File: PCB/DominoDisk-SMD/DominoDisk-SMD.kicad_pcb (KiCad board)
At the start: 4 copper layers, 44 x 32.6 mm, 31 parts, among them J1 Daisy port out, J2 ICSP_ISP6, J3 Daisy port in, J4 UART, K1 TF-104 MicroSD card holder, U1 PC817C-S, U2 ATmega328P-AU, U3 TXB0104PWR level shifter, U4 SE5218ALG voltage regulator, Y1 CSTNE16M0V530000R0 Resonator

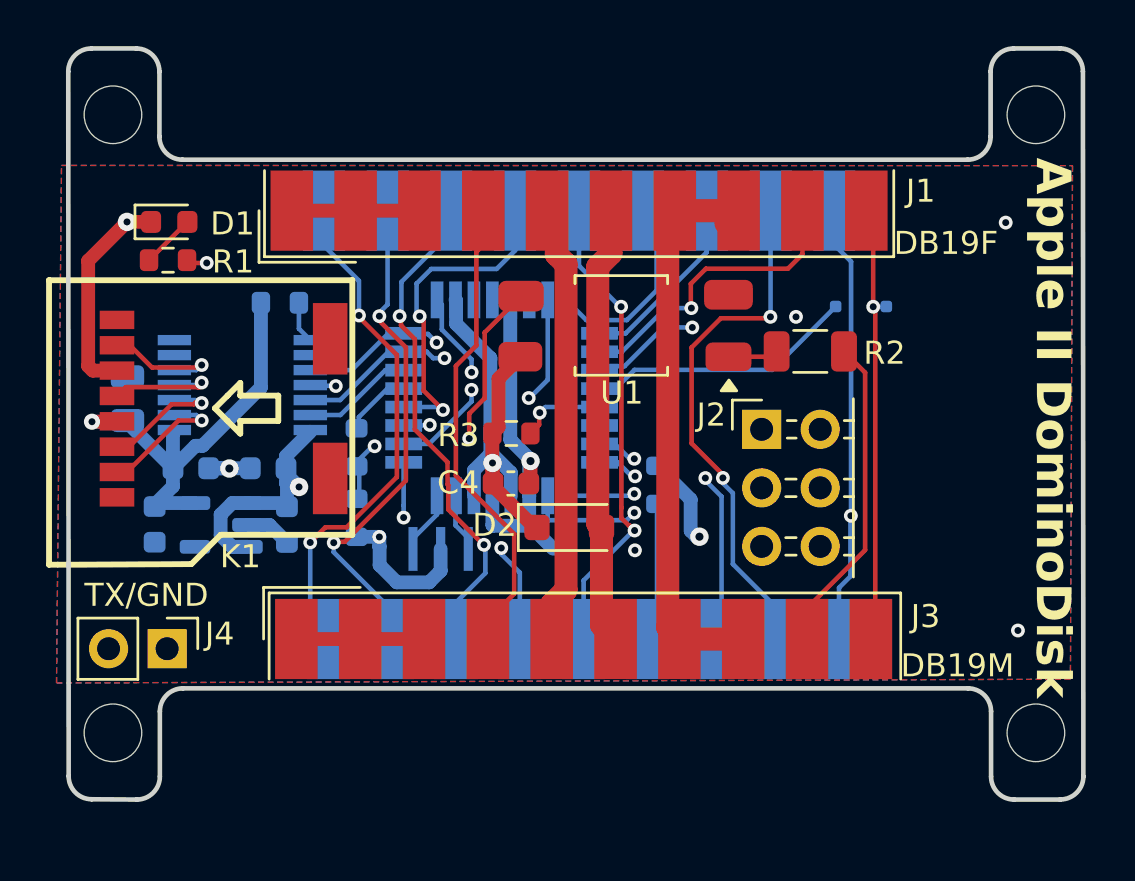
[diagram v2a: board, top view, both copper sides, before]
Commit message: Silkscreen/via avoidance
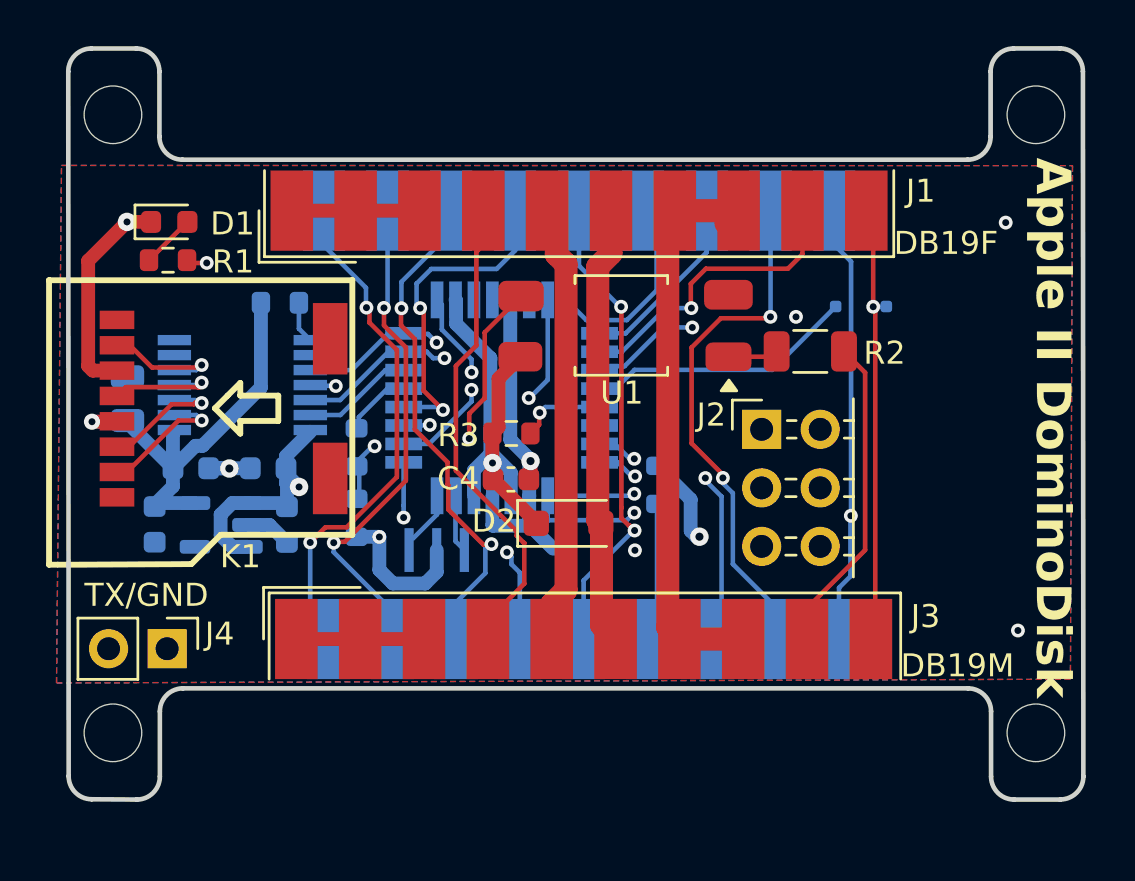
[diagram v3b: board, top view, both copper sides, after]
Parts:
- moved D2 0.18 mm to (121.6, 59.9)
- moved C4 0.18 mm to (119.1, 58.0)
- moved Y1 0.18 mm to (115.9, 61.1)

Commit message: Add via/silkscreen DRC
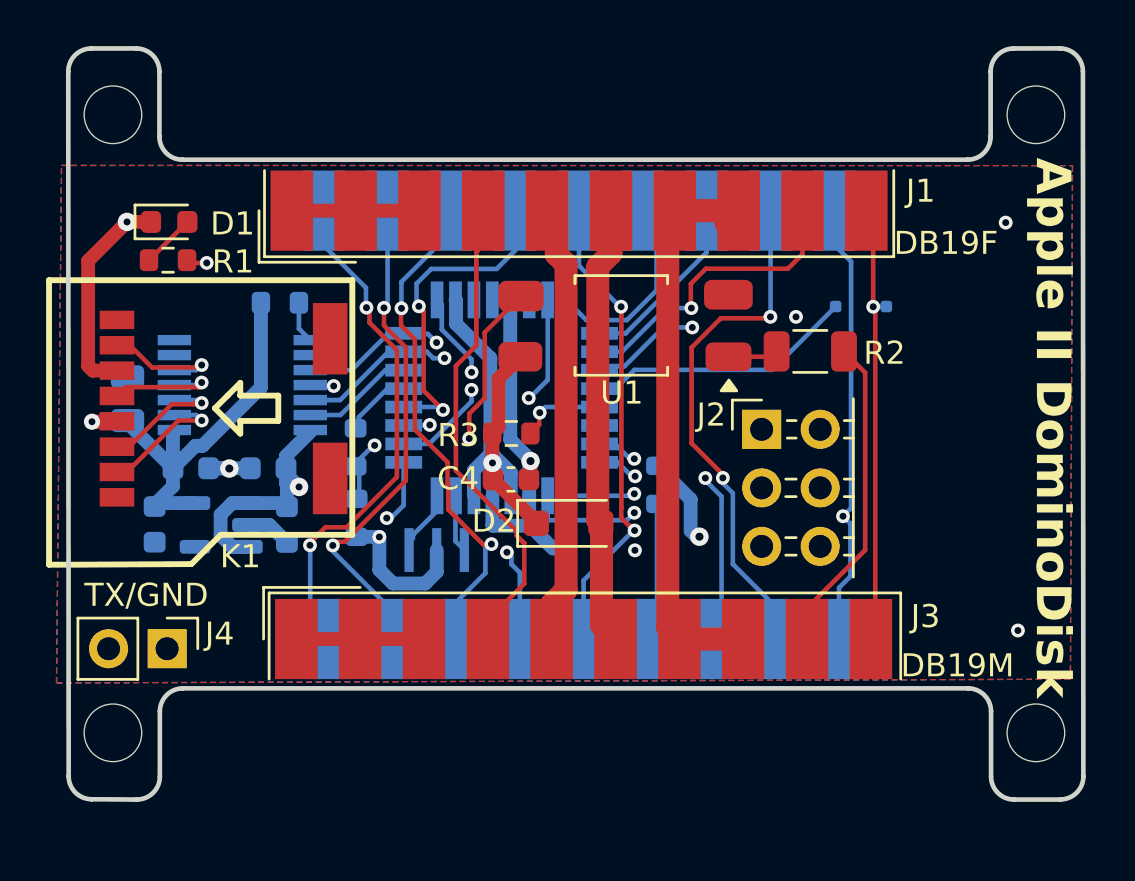
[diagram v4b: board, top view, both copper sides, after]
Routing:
- net PH3_in: track 11.7 -> 12.9 mm

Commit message: Make a full ground plane
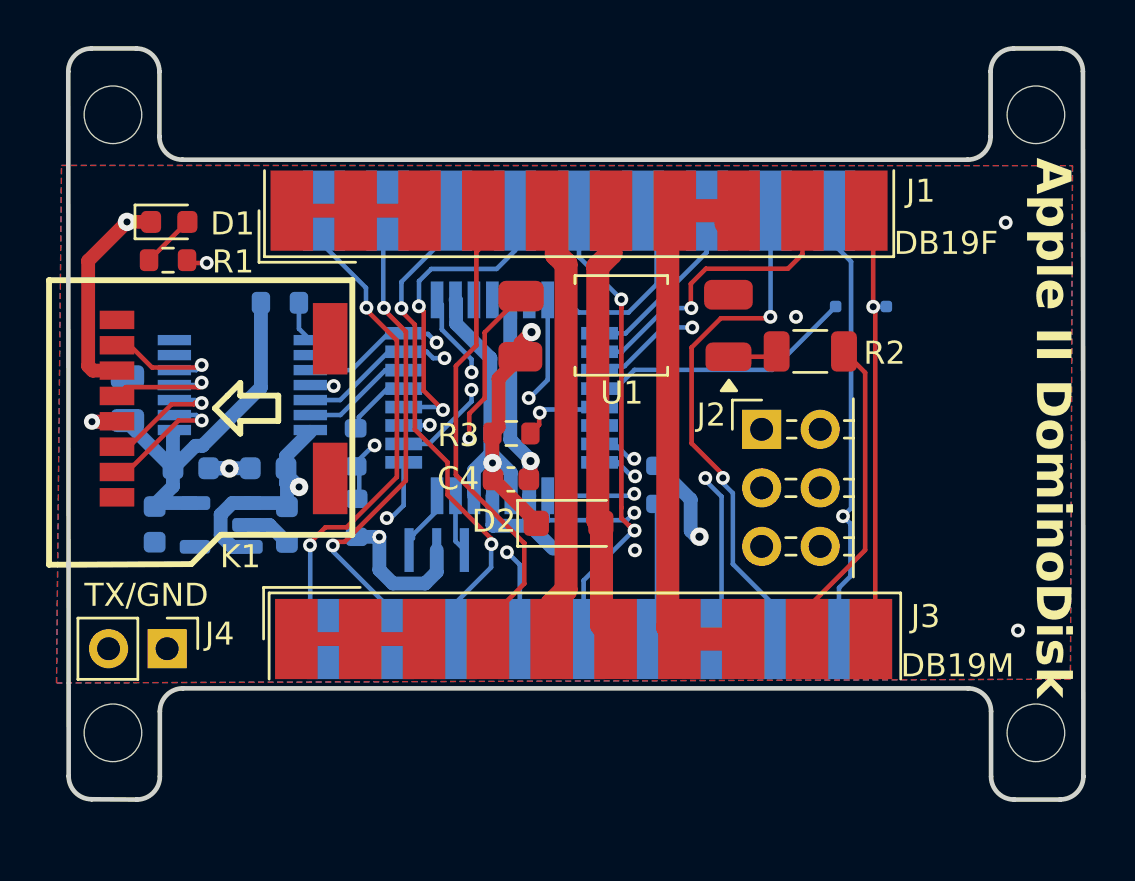
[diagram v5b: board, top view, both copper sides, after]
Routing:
- net LED: track 28.4 -> 27.7 mm
- net 5V_burgerDisk: track 56.9 -> 56.4 mm, vias 2 -> 3

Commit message: Update details
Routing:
- net WRDATA: track 42.9 -> 38.6 mm
- net 5V_burgerDisk: track 56.4 -> 59.9 mm
- net PH2: track 33.9 -> 31.5 mm
- net GND: track 50.8 -> 49.2 mm
- net PH0: track 38.1 -> 36.4 mm
- net RESET: track 15.5 -> 14.4 mm
- net PH3_out: track 14.3 -> 13.3 mm
- net DRV1_in: track 20.6 -> 19.7 mm
- net Net-(R5-Pad2): track 13.5 -> 14.3 mm
- net Net-(U2-XTAL2/PB7): track 2.29 -> 1.64 mm

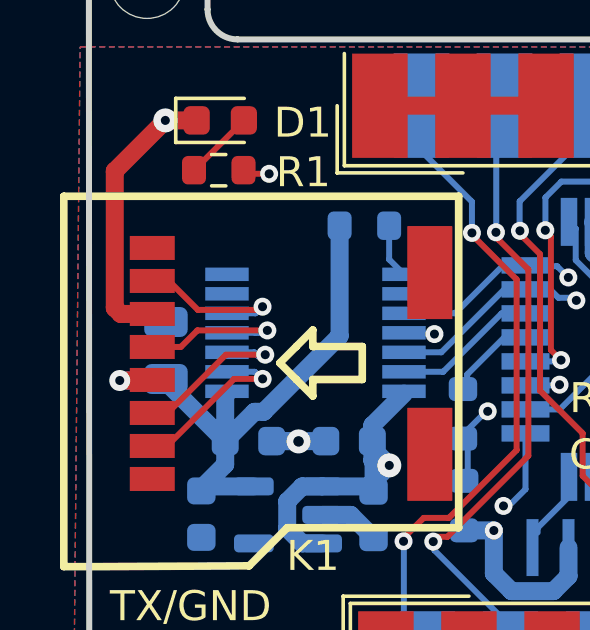
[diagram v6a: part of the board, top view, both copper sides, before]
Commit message: Fix details on DD/angled
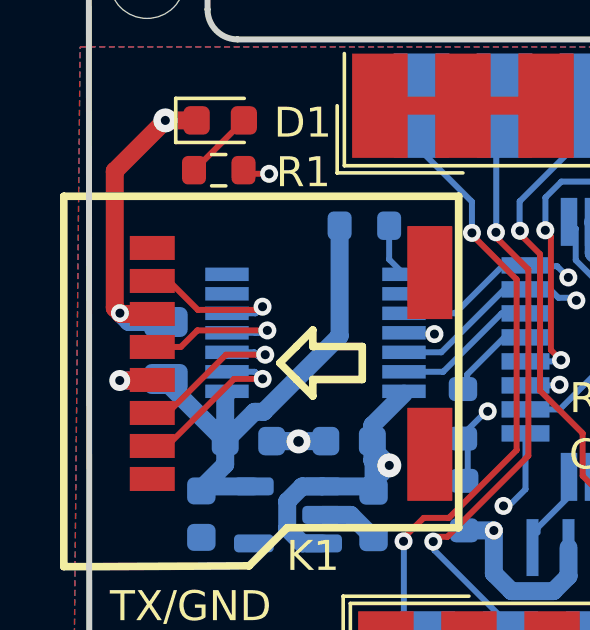
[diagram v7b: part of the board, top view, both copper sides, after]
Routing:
- net GND: track 49.2 -> 50.8 mm, vias 9 -> 10
